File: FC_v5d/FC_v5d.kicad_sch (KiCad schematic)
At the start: 76 parts, among them IC3 RV-3028-C7_32.768kHz_1ppm_TA_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, J1 Conn_01x02, J12 USB_C_Receptacle_USB2.0_16P, J16 DEBUG, J18 Payload, J22 SWD Port, J3 Life Makes Lemonade, J5 BM04B-SRSS-TB(LF)(SN), J6 Conn_Coaxial, SW1 KMR2, SW2 KMR2, U12 TCA9548ARGERQ1, U14 TCA4307DGKR, U2 ZDSD04GLGEAG, U30 E28-2G4M27S, U4 RFM98PW, U7 LSM6DSOTR, U8 LSM303AGRTR

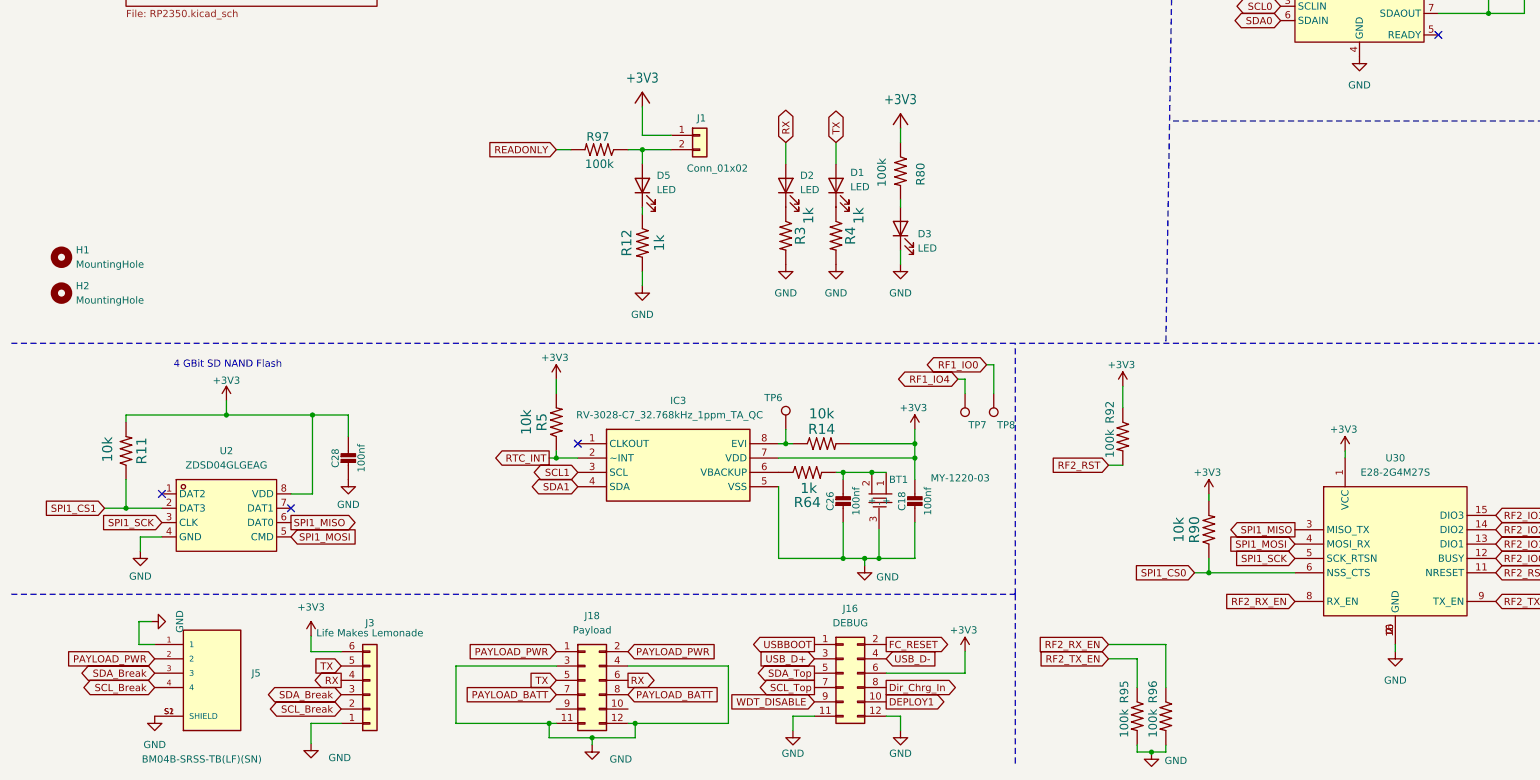
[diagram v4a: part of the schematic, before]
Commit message: Added TX1 and RX1
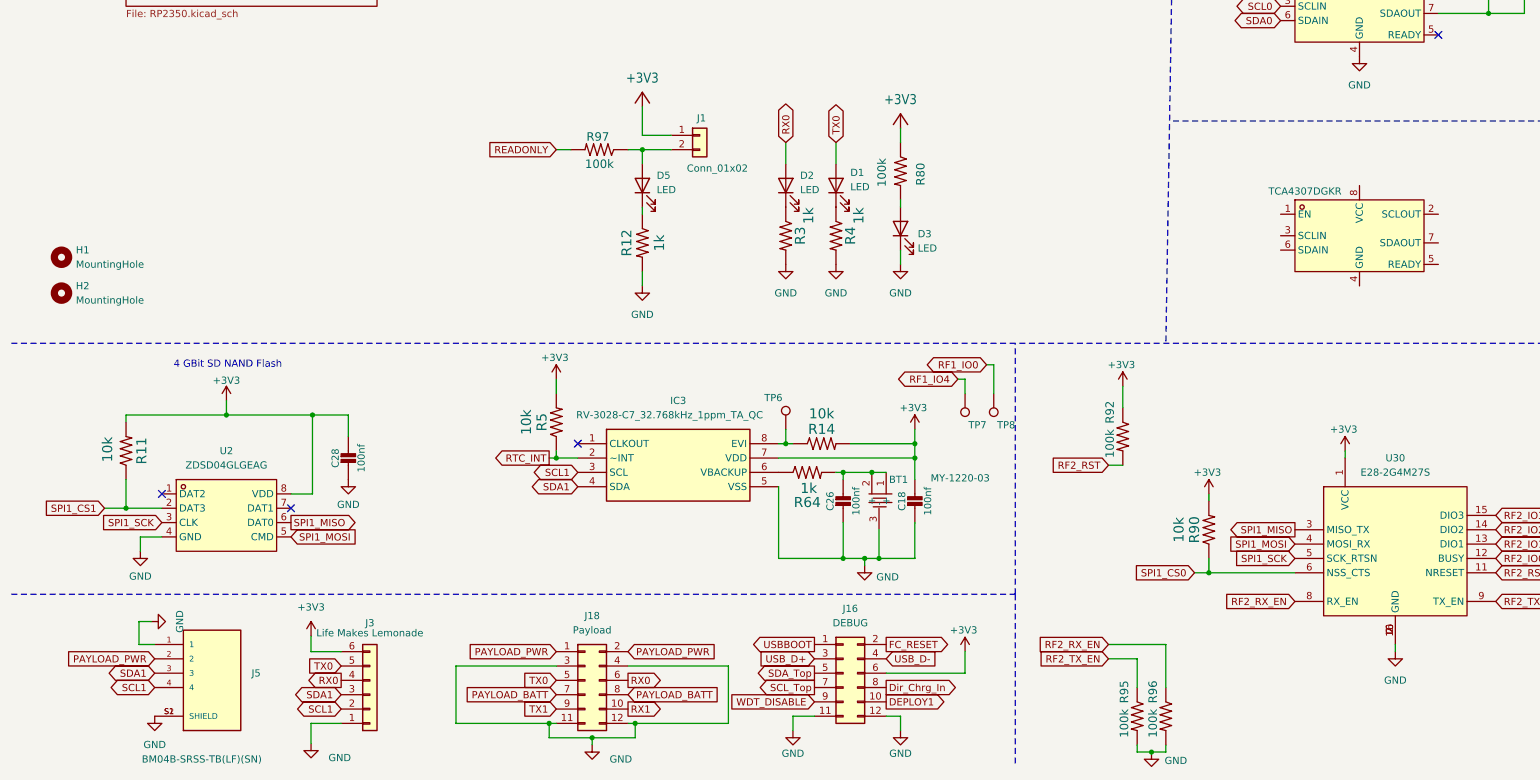
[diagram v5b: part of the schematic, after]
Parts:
- added U15: TCA4307DGKR, easyeda2kicad:VSSOP-8_L3.0-W3.0-P0.65-LS4.9-BL, symbol easyeda2kicad:TCA4307DGKR
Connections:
- net SCL_Break is gone; now on net SCL1: J3.2 (Pin_2), J5.4
- net SDA_Break is gone; now on net SDA1: J3.3 (Pin_3), J5.3
- net RX1: now reaches J18.10 (Pin_10)
- net TX1: now reaches J18.9 (Pin_9)
- net RX renamed RX0
- net TX renamed TX0
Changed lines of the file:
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@@
 		)
 	)
-	(global_label "SDA_Break"
+	(global_label "SDA1"
 		(shape bidirectional)
 		(at 36.83 267.97 180)
@@
 		)
 		(property "Intersheetrefs" "${INTERSHEET_REFS}"
-			(at 22.8759 267.97 0)
+			(at 27.9559 267.97 0)
 			(effects
 				(font
@@
 		)
 	)
-	(global_label "SCL_Break"
+	(global_label "SCL1"
 		(shape bidirectional)
 		(at 69.85 274.32 180)
@@
 		)
 		(property "Intersheetrefs" "${INTERSHEET_REFS}"
-			(at 55.9564 274.32 0)
+			(at 61.0364 274.32 0)
 			(effects
 				(font
@@
 		)
 	)
-	(global_label "TX"
+	(global_label "RX1"
+		(shape output)
+		(at 120.65 274.32 0)
+		(fields_autoplaced yes)
+		(effects
+			(font
+				(size 1.27 1.27)
+			)
+			(justify left)
+		)
+		(property "Intersheetrefs" "${INTERSHEET_REFS}"
+			(at 127.3242 274.32 0)
+			(effects
+				(font
+					(size 1.27 1.27)
+				)
+				(justify left)
+				(hide yes)
+			)
+		)
+	)
+	(global_label "TX0"
 		(shape bidirectional)
 		(at 157.48 173.99 90)
@@
 		)
 		(property "Intersheetrefs" "${INTERSHEET_REFS}"
-			(at 157.48 167.7164 90)
+			(at 157.48 166.5069 90)
 			(effects
 				(font
@@
 		)
 	)
-	(global_label "RX"
+	(global_label "RX0"
 		(shape output)
 		(at 120.65 269.24 0)
@@
 		)
 		(property "Intersheetrefs" "${INTERSHEET_REFS}"
-			(at 126.1147 269.24 0)
+			(at 127.3242 269.24 0)
 			(effects
 				(font
@@
 		)
 	)
+	(global_label "TX1"
+		(shape input)
+		(at 107.95 274.32 180)
+		(fields_autoplaced yes)
+		(effects
+			(font
+				(size 1.27 1.27)
+			)
+			(justify right)
+		)
+		(property "Intersheetrefs" "${INTERSHEET_REFS}"
+			(at 101.5782 274.32 0)
+			(effects
+				(font
+					(size 1.27 1.27)
+				)
+				(justify right)
+				(hide yes)
+			)
+		)
+	)
 	(global_label "SPI0_MISO"
 		(shape output)
@@
 		)
 	)
-	(global_label "TX"
+	(global_label "TX0"
 		(shape input)
 		(at 107.95 269.24 180)
@@
 		)
 		(property "Intersheetrefs" "${INTERSHEET_REFS}"
-			(at 103.3598 269.1606 0)
+			(at 101.5782 269.24 0)
 			(effects
 				(font
@@
 		)
 	)
-	(global_label "SCL_Break"
+	(global_label "SCL1"
 		(shape bidirectional)
 		(at 36.83 270.51 180)
@@
 		)
 		(property "Intersheetrefs" "${INTERSHEET_REFS}"
-			(at 22.9364 270.51 0)
+			(at 28.0164 270.51 0)
 			(effects
 				(font
@@
 		)
 	)
-	(global_label "TX"
+	(global_label "TX0"
 		(shape input)
 		(at 69.85 266.7 180)
@@
 		)
 		(property "Intersheetrefs" "${INTERSHEET_REFS}"
-			(at 65.2598 266.6206 0)
+			(at 63.4782 266.7 0)
 			(effects
 				(font
@@
 		)
 	)
-	(global_label "RX"
+	(global_label "RX0"
 		(shape bidirectional)
 		(at 148.59 173.99 90)
@@
 		)
 		(property "Intersheetrefs" "${INTERSHEET_REFS}"
-			(at 148.59 167.414 90)
+			(at 148.59 166.2045 90)
 			(effects
 				(font
@@
 		)
 	)
-	(global_label "SDA_Break"
+	(global_label "SDA1"
 		(shape bidirectional)
 		(at 69.85 271.78 180)
@@
 		)
 		(property "Intersheetrefs" "${INTERSHEET_REFS}"
-			(at 55.8959 271.78 0)
+			(at 60.9759 271.78 0)
 			(effects
 				(font
@@
 		)
 	)
-	(global_label "RX"
+	(global_label "RX0"
 		(shape output)
 		(at 69.85 269.24 180)
@@
 		)
 		(property "Intersheetrefs" "${INTERSHEET_REFS}"
-			(at 64.9574 269.1606 0)
+			(at 63.1758 269.24 0)
 			(effects
 				(font
@@
 					(unit 1)
 				)
+			)
+		)
+	)
+	(symbol
+		(lib_id "easyeda2kicad:TCA4307DGKR")
+		(at 250.19 190.5 0)
+		(unit 1)
+		(exclude_from_sim no)
+		(in_bom yes)
+		(on_board yes)
+		(dnp no)
+		(property "Reference" "U15"
+			(at 224.282 192.024 0)
+			(effects
+				(font
+					(size 1.27 1.27)
+				)
+				(hide yes)
+			)
+		)
+		(property "Value" "TCA4307DGKR"
+			(at 240.538 182.626 0)
+			(effects
+				(font
+					(size 1.27 1.27)
+				)
+			)
+		)
+		(property "Footprint" "easyeda2kicad:VSSOP-8_L3.0-W3.0-P0.65-LS4.9-BL"
+			(at 250.19 201.93 0)
+			(effects
+				(font
+					(size 1.27 1.27)
+				)
+				(hide yes)
+			)
+		)
+		(property "Datasheet" "https://www.ti.com/lit/ds/symlink/tca4307.pdf?ts=1756183410246&ref_url=https%253A%252F%252Fwww.ti.com%252Fproduct%252FTCA4307"
+			(at 250.19 190.5 0)
+			(effects
+				(font
+					(size 1.27 1.27)
+				)
+				(hide yes)
+			)
+		)
+		(property "Description" ""
+			(at 250.19 190.5 0)
+			(effects
+				(font
+					(size 1.27 1.27)
+				)
+				(hide yes)
+			)
+		)
+		(property "LCSC Part" "C880333"
+			(at 250.19 204.47 0)
+			(effects
+				(font
+					(size 1.27 1.27)
+				)
+				(hide yes)
+			)
+		)
+		(pin "4"
+		)
+		(pin "1"
+		)
+		(pin "2"
+		)
+		(pin "3"
+		)
+		(pin "6"
+		)
+		(pin "5"
+		)
+		(pin "8"
+		)
+		(pin "7"
+		)
+		(instances
+			(project "FC_v5d"
+				(path "/c64c0d72-a9f6-4f3a-891e-1f647558f538"
+					(reference "U15")
+					(unit 1)
+				)

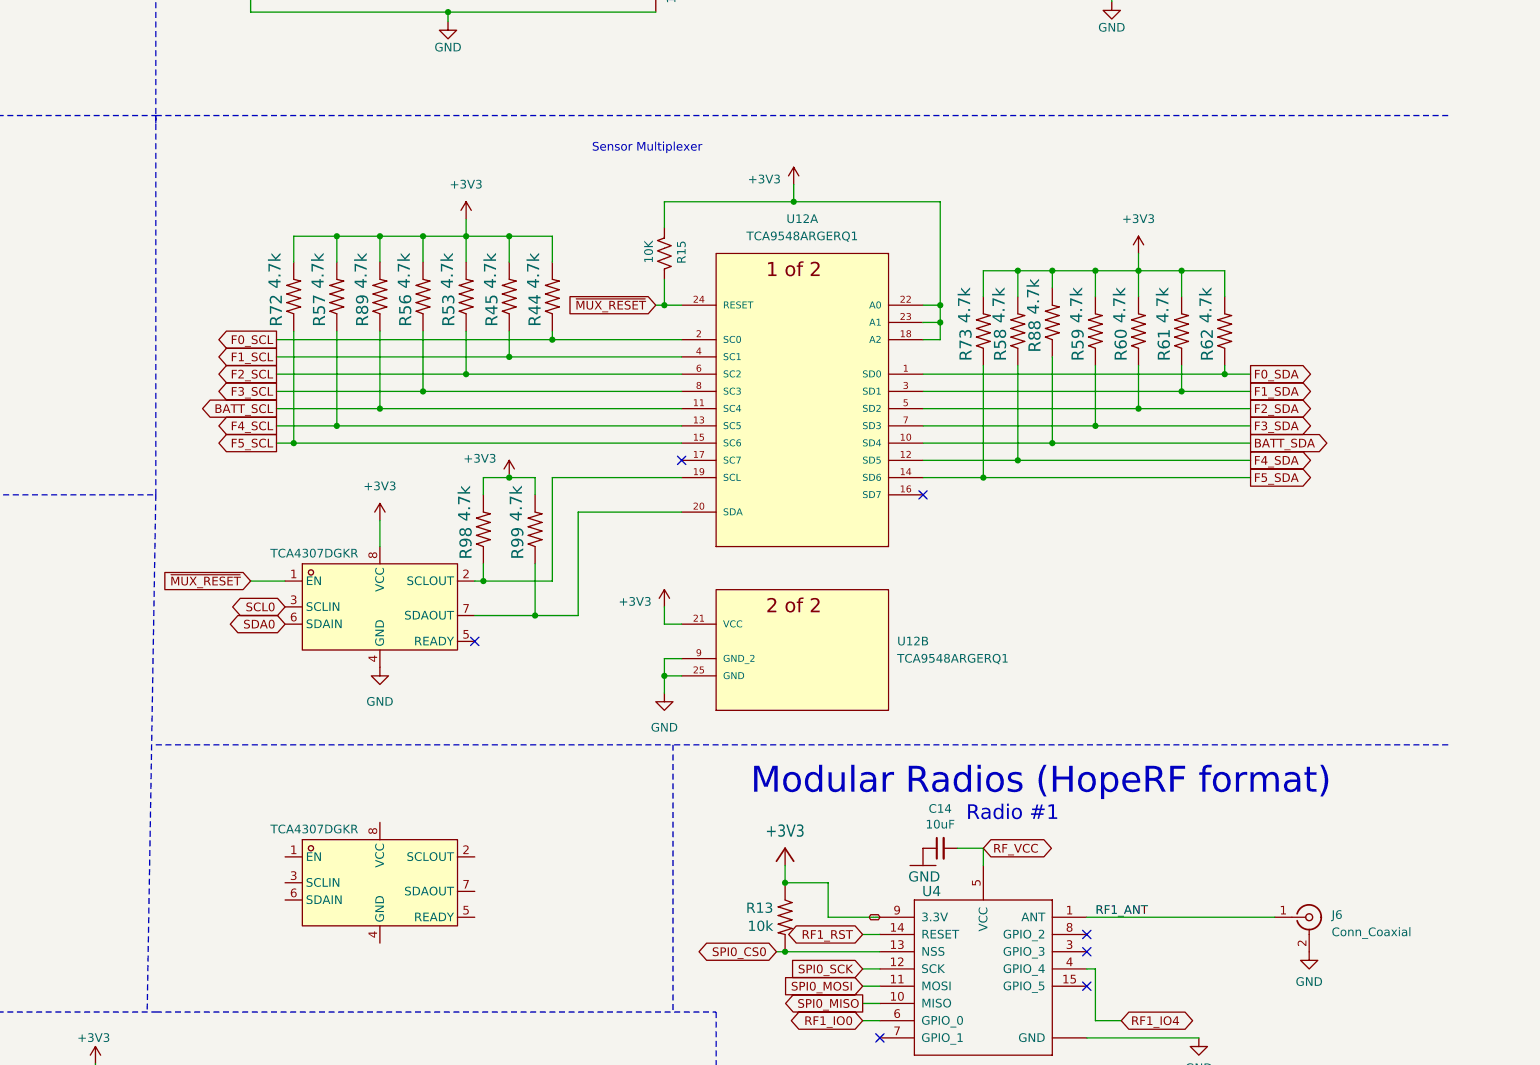
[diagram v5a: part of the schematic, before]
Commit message: Wired up SDA and SCL Top
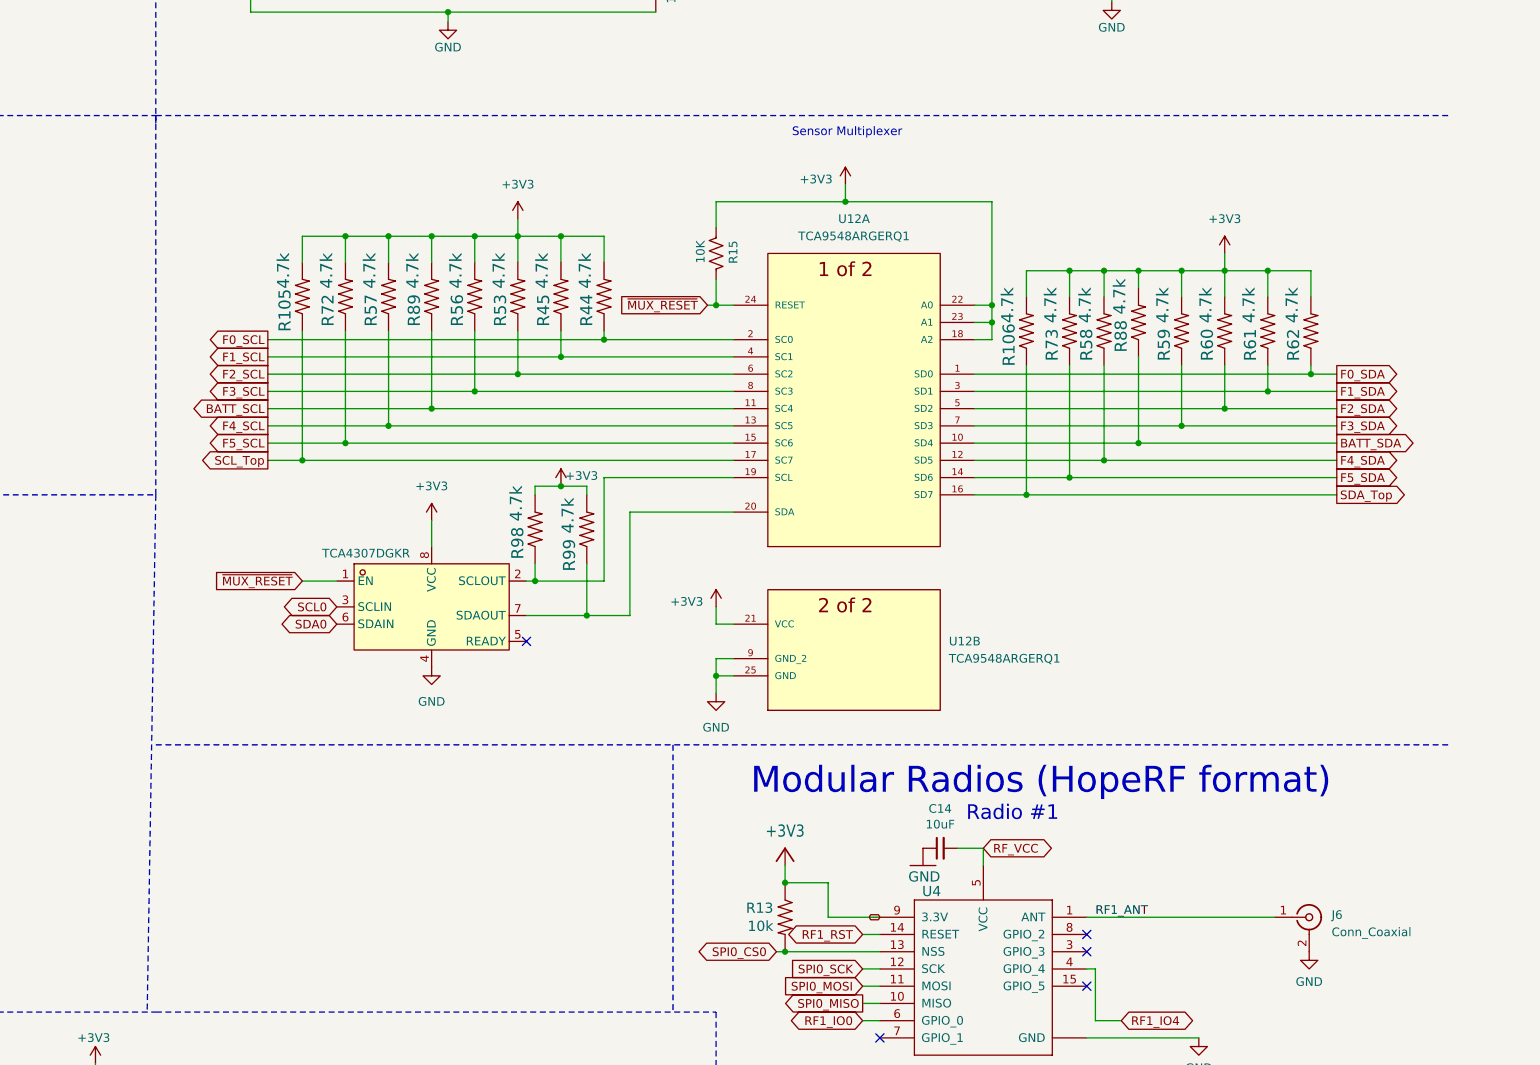
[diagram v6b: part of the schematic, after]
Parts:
- removed U15: TCA4307DGKR, easyeda2kicad:VSSOP-8_L3.0-W3.0-P0.65-LS4.9-BL, symbol easyeda2kicad:TCA4307DGKR
- added R105, R106: 4.7k, Resistor_SMD:R_0603_1608Metric, symbol mainboard:RESISTOR0603
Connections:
- net +3V3: now also R105.2, R106.2
- net SCL_Top: now also U12.17 (SC7), R105.1
- net SDA_Top: now also U12.16 (SD7), R106.1
- no-connect marks 21 -> 19
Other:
- moved on the sheet: R15, R44, R45, R53, R56, R57, R58, R59, R60, R61, R62, R72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

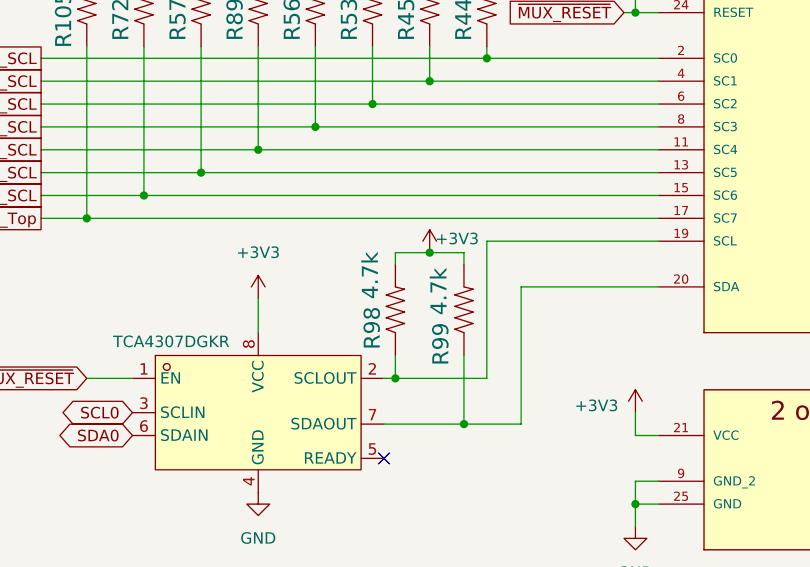
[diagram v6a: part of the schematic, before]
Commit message: Adjusted Pull Up Resistor Values
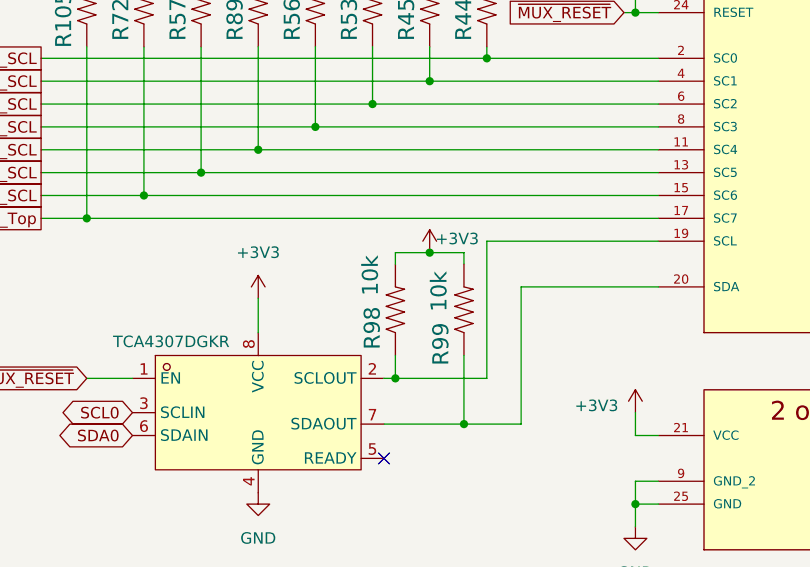
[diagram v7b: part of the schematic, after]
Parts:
- R98, R99: value 4.7k -> 10k
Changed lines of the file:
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@@
 			)
 		)
-		(property "Value" "4.7k"
+		(property "Value" "10k"
 			(at 276.86 136.398 0)
 			(effects
@@
 			)
 		)
-		(property "Value" "4.7k"
+		(property "Value" "10k"
 			(at 269.24 134.62 0)
 			(effects
